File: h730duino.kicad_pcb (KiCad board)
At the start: 4 copper layers, 101.6 x 53.3 mm, 114 parts, among them J1 USB_C_Receptacle_USB2.0, J2 USB_B_Micro, J3 L834-1G1T-91, J4 105162-0001, P1 Digital, P10 CONN_01X01, P11 CONN_01X01, P13 CONN_01X01, P2 Power, P3 Analog, P4 Analog, P5 PWM, P6 PWM, P7 Communication, P8 CONN_01X01, P9 EXT, SW1 RESET, U1 STM32H730ZBT6, U10 APS6404L-3SQN, U12 AP22814BW5, U2 W25Q32JVSS, U3 AP63203WU, U4 AP63205WU, U5 MAX40200AUK, U6 MAX40200AUK, U7 STM32F042F6Px, U8 MAX40200AUK, U9 LAN8742A, Y1 32.768K, Y2 8M, Y3 25M

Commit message: Add SWD connector for cortex-m7, SWD poggo pins and boot jumper for cmsis-dap mcu.
Signed-off-by: Martin Ribelotta <martinribelotta@gmail.com>
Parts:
- added J5: Conn_ARM_JTAG_SWD_10, Connector_PinHeader_1.27mm:PinHeader_2x05_P1.27mm_Vertical_SMD, F.Cu at (153.5, 98.4)
- added J6: Conn_ARM_JTAG_SWD_10, Connector:Tag-Connect_TC2050-IDC-NL_2x05_P1.27mm_Vertical, F.Cu at (142.3, 101.0)
- added JP2: Jumper_NO_Small, Connector_PinHeader_2.54mm:PinHeader_1x02_P2.54mm_Vertical, F.Cu at (131.6, 102.0)
- moved LOGO1 43.6 mm to (192.9, 106.6)
- moved G1 38.6 mm to (194.0, 89.3)
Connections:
- U7 pad 19: (no net) -> /Debug/DBG_SWDIO
- U7 pad 20: (no net) -> /Debug/DBG_SWCK
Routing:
- net /Debug/DBG_SWCK: track 0.00 -> 34.9 mm
- net /Debug/DBG_SWDIO: track 0.00 -> 32.2 mm
- net /Debug/~DBGR: track 4.21 -> 34.7 mm, vias 0 -> 2
- net GND: track 141.4 -> 152.2 mm, vias 74 -> 77
- net /Debug/DBGB: track 5.46 -> 15.7 mm
- net /~RST: track 105.1 -> 114.8 mm, vias 3 -> 4
- net /SWCLK: track 71.9 -> 77.4 mm, vias 2 -> 3
- net +3V3: track 68.4 -> 72.4 mm, vias 28 -> 30
- net /EXT1: track 68.8 -> 64.9 mm
- net /EXT8: track 32.4 -> 28.9 mm
- net /EXT7: track 35.2 -> 31.6 mm
- net /EXT6: track 37.9 -> 34.4 mm
- net /EXT5: track 44.3 -> 40.7 mm
- net /EXT4: track 47.0 -> 43.5 mm
- net /EXT3: track 49.8 -> 46.2 mm
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
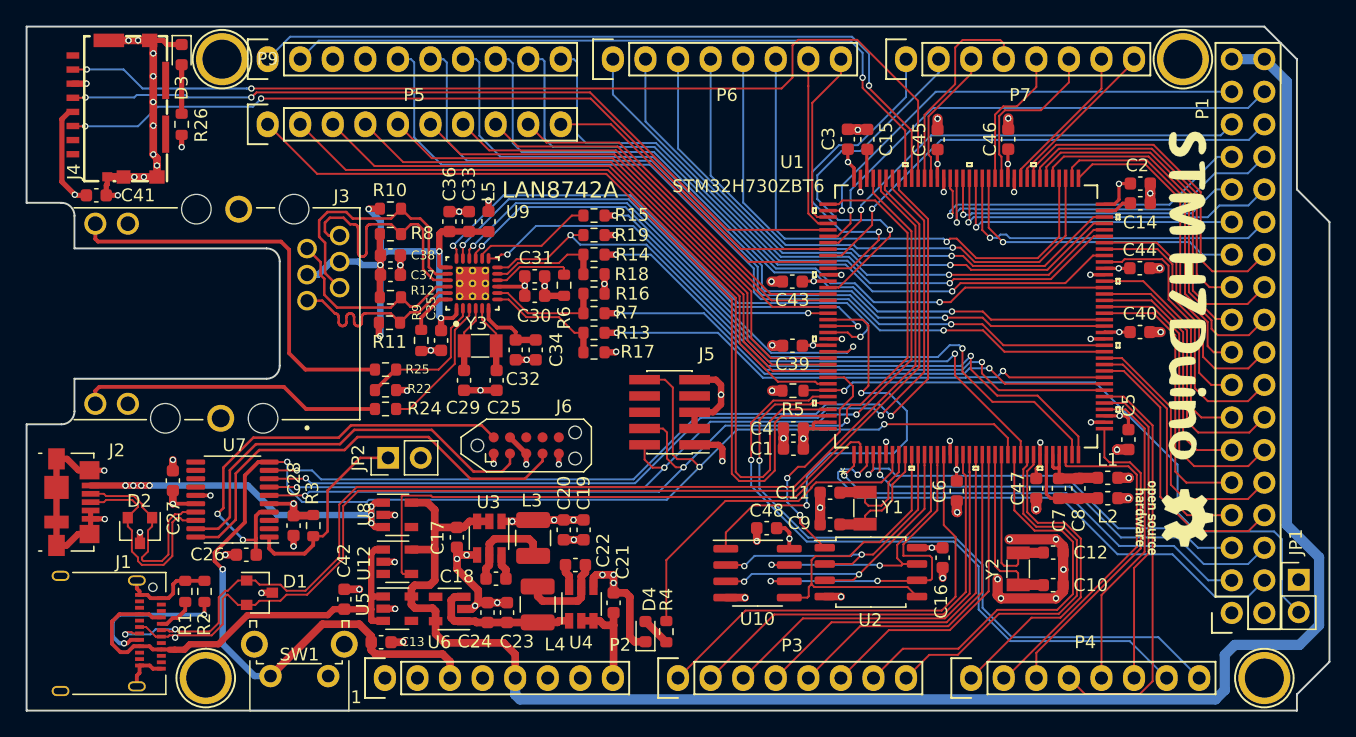
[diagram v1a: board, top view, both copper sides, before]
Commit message: Replace non stocked components.
 - Redesign 5V/3.3V using TPS6216xDSGT
 - Use bigger crystal (move to 5031 case)
 - Change some components parts

Signed-off-by: Martin Ribelotta <martinribelotta@gmail.com>
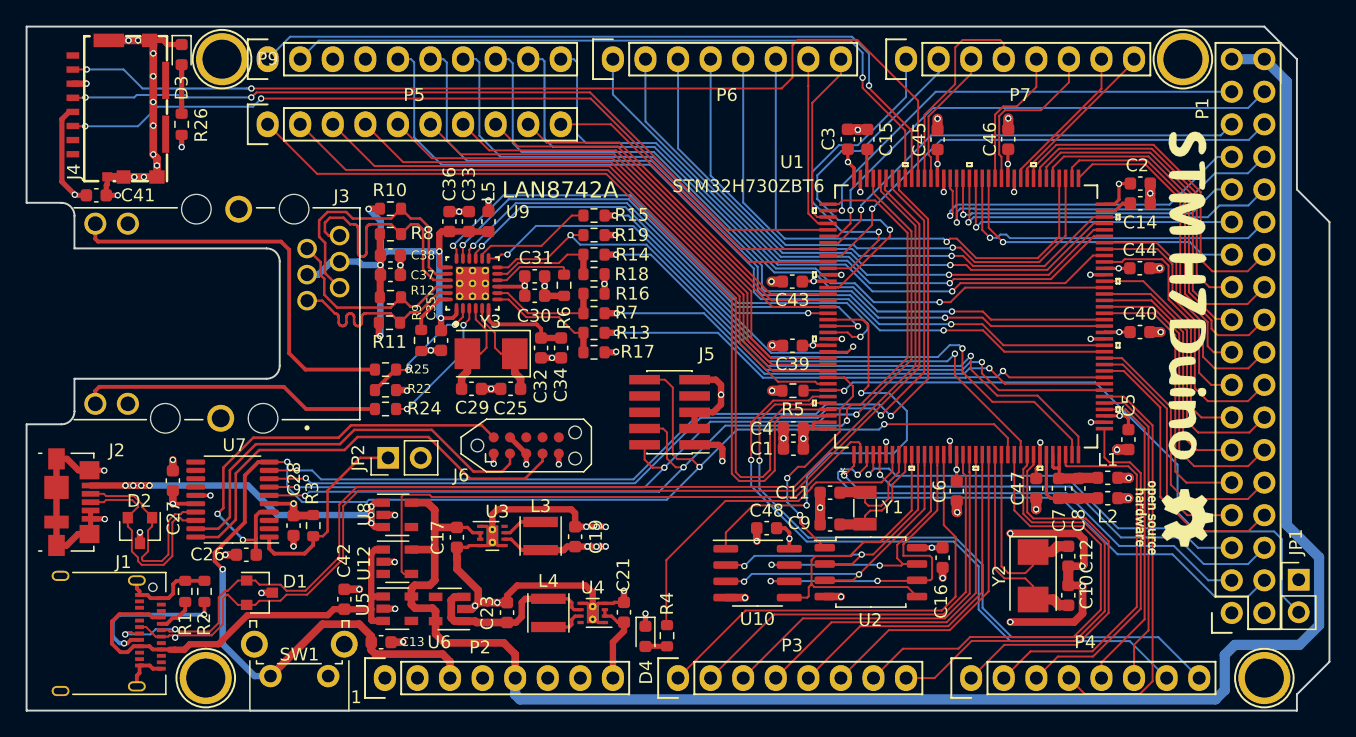
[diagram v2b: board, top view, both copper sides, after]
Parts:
- removed C18, C22: 100n, Capacitor_SMD:C_0603_1608Metric
- removed C20, C24: 2.2u, Capacitor_SMD:C_0603_1608Metric
- C19, C23: value 2.2u -> 22u
- C32: value 420p -> 470p
- L3, L4: value 4.7u -> NR3015T2R2M; footprint Inductor_SMD:L_1210_3225Metric -> Inductor_SMD:L_Taiyo-Yuden_MD-3030
- U3: value AP63203WU -> TPS62162DSG; footprint Package_TO_SOT_SMD:TSOT-23-6 -> Package_SON:WSON-8-1EP_2x2mm_P0.5mm_EP0.9x1.6mm_ThermalVias
- U4: value AP63205WU -> TPS62163DSG; footprint Package_TO_SOT_SMD:TSOT-23-6 -> Package_SON:WSON-8-1EP_2x2mm_P0.5mm_EP0.9x1.6mm_ThermalVias
- Y2, Y3: footprint footprints:Crystal_SMD_3215-2Pin_3.2x1.5mm -> Crystal:Crystal_SMD_5032-2Pin_5.0x3.2mm
- moved C32 1.99 mm to (143.5, 93.4)
- moved C34 1.99 mm to (145.1, 93.4)
- moved C10 1.42 mm to (184.6, 112.7), turned to 90 degrees
- moved Y2 1.28 mm to (181.9, 111.2), turned to 270 degrees
- moved C25 1.28 mm to (141.1, 96.6), turned to 0 degrees
- moved C12 1.21 mm to (184.6, 109.6), turned to 270 degrees
- moved U4 1.13 mm to (147.5, 114.0), turned to 180 degrees
- moved C21 1.10 mm to (150.0, 114.0)
- moved L4 1.07 mm to (144.1, 114.0), turned to 90 degrees
- moved Y3 1.05 mm to (139.6, 93.8), turned to 180 degrees
- moved C29 0.88 mm to (138.1, 96.6), turned to 180 degrees
- moved C19 0.85 mm to (146.2, 108.1), turned to 90 degrees
- moved L3 0.60 mm to (143.5, 108.1), turned to 270 degrees
- moved D4 0.37 mm to (151.6, 115.9), turned to 270 degrees
- moved R4 0.32 mm to (153.3, 115.8)
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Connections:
- L3 pad 1: Net-(C18-Pad1) -> Net-(L3-Pad1)
- L4 pad 1: Net-(C22-Pad1) -> Net-(L4-Pad1)
- U3 pad 1: +3V3 -> GND
- U3 pad 5: Net-(C18-Pad1) -> GND
- U3 pad 6: Net-(C18-Pad2) -> +3V3
- U4 pad 1: /5Vreg -> GND
- U4 pad 5: Net-(C22-Pad1) -> GND
- U4 pad 6: Net-(C22-Pad2) -> /5Vreg
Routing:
- net GND: track 152.2 -> 177.5 mm, vias 77 -> 74
- net Net-(C18-Pad1): track 7.54 -> 0.00 mm
- net Net-(C22-Pad1): track 7.09 -> 0.00 mm
- net /A8: track 25.5 -> 30.4 mm
- net /A7: track 30.1 -> 35.0 mm
- net /A6: track 32.3 -> 37.2 mm
- net Net-(L3-Pad1): track 0.00 -> 3.16 mm
- net Net-(L4-Pad1): track 0.00 -> 3.09 mm
- net Net-(C12-Pad1): track 12.7 -> 15.6 mm
- net Net-(C25-Pad2): track 5.30 -> 8.15 mm
- net /5Vreg: track 11.9 -> 14.7 mm
- net Net-(C29-Pad2): track 5.21 -> 8.03 mm
- net Net-(C10-Pad1): track 13.6 -> 16.4 mm
- net /A9: track 26.9 -> 29.7 mm
- net Net-(C32-Pad1): track 5.55 -> 7.56 mm
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
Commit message: Reorder power supply
Signed-off-by: Martin Ribelotta <martinribelotta@gmail.com>
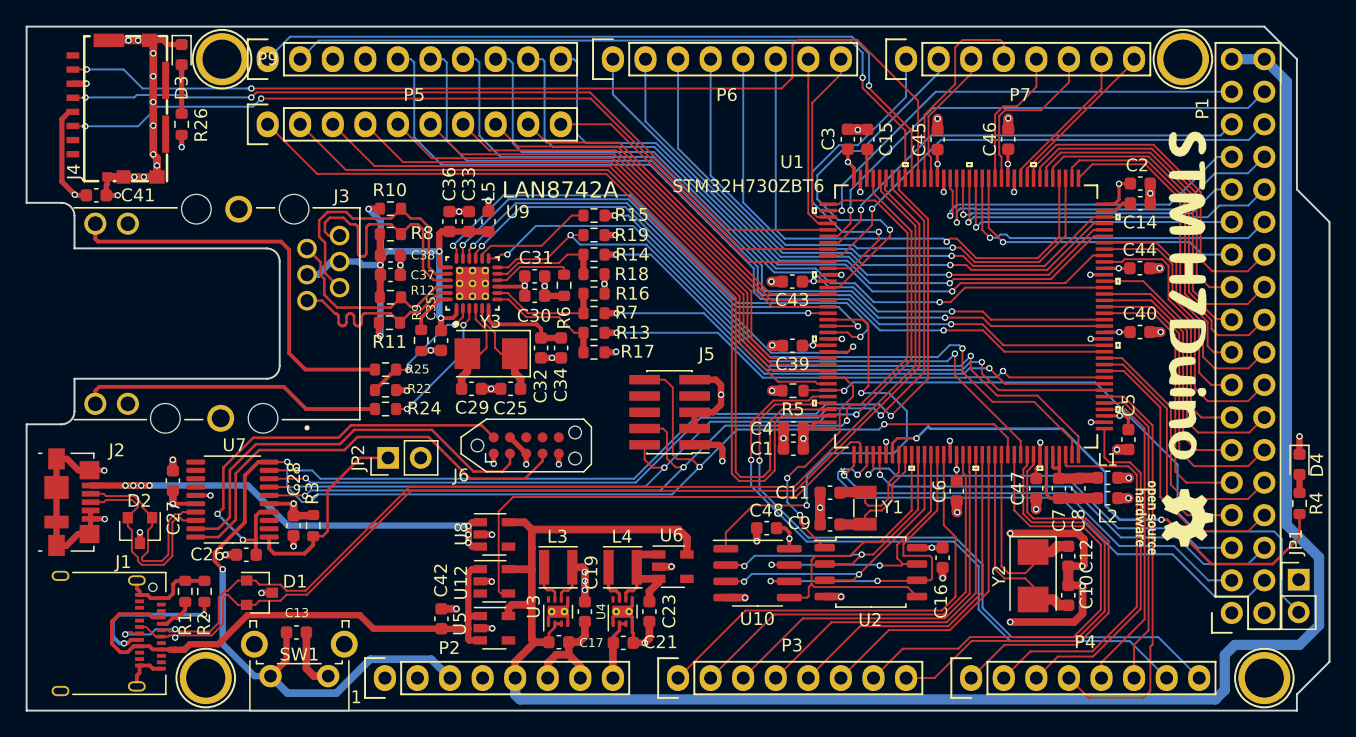
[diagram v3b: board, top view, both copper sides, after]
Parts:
- moved D4 52.7 mm to (202.6, 102.5)
- moved R4 50.4 mm to (202.6, 105.5), turned to 270 degrees
- moved U6 17.7 mm to (153.8, 110.4), turned to 0 degrees
- moved C17 11.4 mm to (144.9, 116.3), turned to 0 degrees
- moved C23 11.1 mm to (151.9, 113.9), turned to 270 degrees
- moved U3 7.81 mm to (144.8, 113.9), turned to 90 degrees
- moved C42 7.72 mm to (135.7, 114.5)
- moved U12 7.72 mm to (139.9, 111.6)
- moved U5 7.72 mm to (139.9, 115.2)
- moved U8 7.72 mm to (139.9, 107.9)
- moved L4 6.80 mm to (149.9, 110.5), turned to 0 degrees
- moved C13 6.65 mm to (124.4, 115.6)
- moved C19 5.89 mm to (146.9, 113.9), turned to 270 degrees
- moved L3 2.80 mm to (144.8, 110.5), turned to 0 degrees
- moved C21 2.39 mm to (149.9, 116.4), turned to 0 degrees
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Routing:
- net GND: track 177.5 -> 162.2 mm, vias 74 -> 69
- net /USR_LED: track 26.9 -> 41.8 mm, vias 0 -> 2
- net /DBG_VBUS: track 29.4 -> 37.3 mm
- net VBUS: track 36.6 -> 44.4 mm
- net /~USB_ON: track 45.3 -> 38.4 mm
- net +5V: track 146.1 -> 152.4 mm
- net /5Vreg: track 14.7 -> 9.52 mm
- net /USB_OTG_HS_P: track 92.9 -> 90.5 mm
- net /USB_OTG_HS_N: track 90.1 -> 87.7 mm
- net /Vin: track 6.90 -> 4.94 mm
- net +3V3: track 74.4 -> 72.6 mm
- net /~RST: track 114.8 -> 116.1 mm
- net /A11: track 32.1 -> 32.7 mm

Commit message: Fix in design:
 - Add r-series to QSPI interfaces
 - Change vCAP from 100n to 2.2u
 - Add pullup to SWCK/DIO and nRST
 - Remove AGND/DGND separation

Signed-off-by: Martin Ribelotta <martinribelotta@gmail.com>
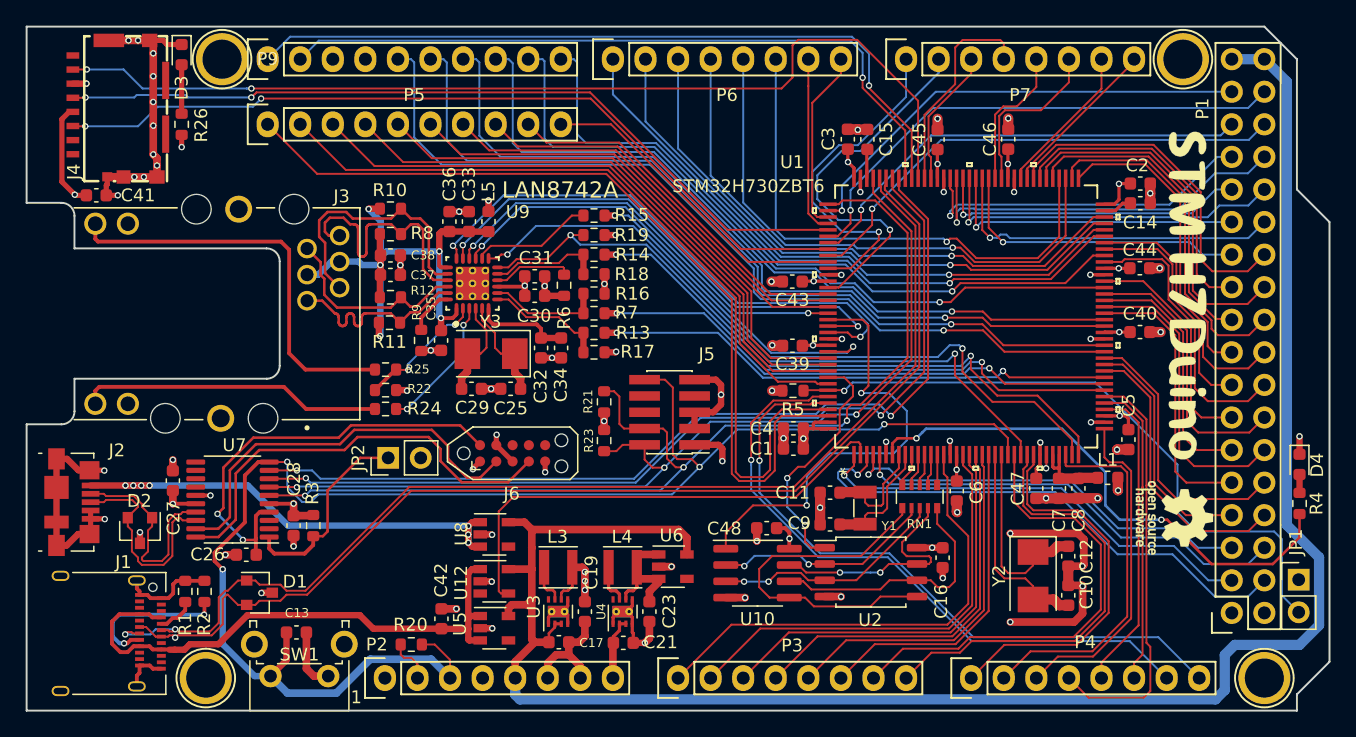
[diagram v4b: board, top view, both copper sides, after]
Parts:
- removed L2: ferrite, Inductor_SMD:L_0603_1608Metric
- added R20: 10K, Resistor_SMD:R_0603_1608Metric, F.Cu at (133.4, 116.5)
- added R21: 10K, Resistor_SMD:R_0603_1608Metric, F.Cu at (148.4, 97.6)
- added R23: 10K, Resistor_SMD:R_0603_1608Metric, F.Cu at (148.4, 100.6)
- added RN1: R_Pack05, Resistor_SMD:R_Array_Convex_5x0603, F.Cu at (173.0, 105.0)
- C14, C15: value 100n -> 2.2u
- R3, R5: value 1K5 -> 10K
- moved J6 1.23 mm to (141.3, 101.6)
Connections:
- C7 pad 2: GNDA -> GND
- C8 pad 2: GNDA -> GND
- U1 pad 10: /OCTOSPIM_P2_IO0 -> Net-(RN1-Pad10)
- U1 pad 11: /OCTOSPIM_P2_IO1 -> Net-(RN1-Pad9)
- U1 pad 12: /OCTOSPIM_P2_IO2 -> Net-(RN1-Pad8)
- U1 pad 13: /OCTOSPIM_P2_IO3 -> Net-(RN1-Pad7)
- U1 pad 14: /OCTOSPIM_P2_CLK -> Net-(RN1-Pad6)
- U1 pad 31: GNDA -> GND
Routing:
- net GNDA: track 7.21 -> 0.00 mm
- net /OCTOSPIM_P2_IO1: track 24.3 -> 17.2 mm
- net /OCTOSPIM_P2_CLK: track 27.0 -> 20.2 mm, vias 2 -> 0
- net /OCTOSPIM_P2_IO2: track 25.0 -> 18.4 mm
- net /SWCLK: track 77.4 -> 83.0 mm
- net +3V3: track 72.6 -> 77.7 mm, vias 30 -> 31
- net GND: track 162.2 -> 166.3 mm, vias 69 -> 70
- net /~RST: track 116.1 -> 120.3 mm
- net /OCTOSPIM_P2_IO3: track 22.6 -> 18.6 mm
- net /SWDIO: track 72.5 -> 75.9 mm
- net Net-(RN1-Pad10): track 0.00 -> 2.68 mm
- net Net-(RN1-Pad9): track 0.00 -> 2.59 mm
- net Net-(RN1-Pad8): track 0.00 -> 2.53 mm
- net Net-(RN1-Pad7): track 0.00 -> 2.47 mm
- net Net-(RN1-Pad6): track 0.00 -> 2.38 mm
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
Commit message: Major rework:
 - Split flash/ram in two QSPI iface
   - Flash is connected to QSPI2
   - PSRAM is connected to QSPI1
 - Move QSPI PSRAM near to P1
 - Reorder pins to P1 and P5
 - Reasign I2C5, UART4 to more convenient place
 - Reasign PWM pins to more convenient place
 - Rerarrange 25MHz ETHPHY crystal

Signed-off-by: Martin Ribelotta <martinribelotta@gmail.com>
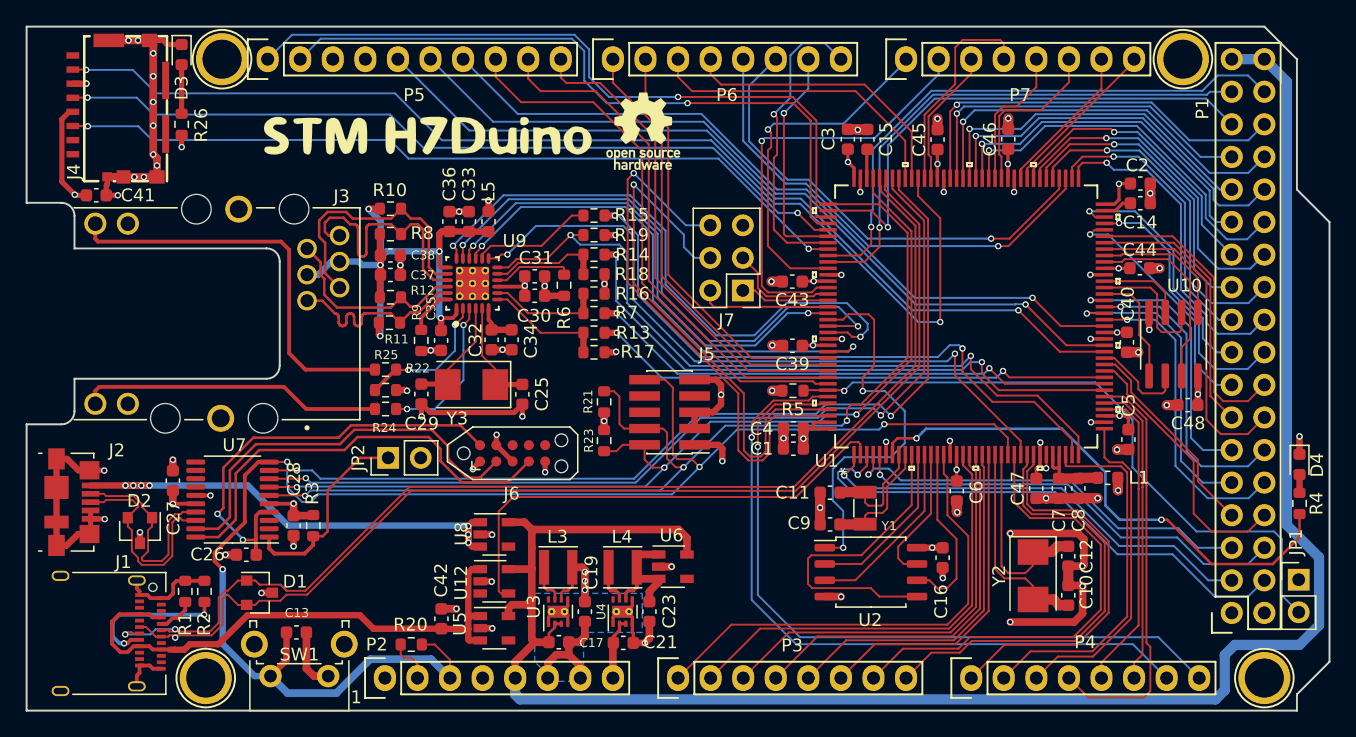
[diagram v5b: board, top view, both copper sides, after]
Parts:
- removed P9: EXT, Socket_Arduino_Mega:Socket_Strip_Arduino_1x10
- removed RN1: R_Pack05, Resistor_SMD:R_Array_Convex_5x0603
- added J7: Conn_02x03_Odd_Even, Connector_PinHeader_2.54mm:PinHeader_2x03_P2.54mm_Vertical, F.Cu at (159.2, 88.9)
- moved G1 60.6 mm to (134.7, 76.8), turned to 0 degrees
- moved LOGO1 51.2 mm to (151.5, 76.5), turned to 0 degrees
- moved U10 37.0 mm to (192.8, 93.1), turned to 270 degrees
- moved C48 34.2 mm to (193.9, 97.8)
- moved C29 3.93 mm to (134.2, 97.0), turned to 90 degrees
- moved C34 3.91 mm to (141.2, 92.7)
- moved C32 3.91 mm to (139.6, 92.7)
- moved Y3 2.85 mm to (138.1, 96.2)
- moved C40 1.29 mm to (189.2, 92.9), turned to 270 degrees
- moved C25 1.01 mm to (142.0, 97.0), turned to 90 degrees
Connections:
- U1 pad 10: Net-(RN1-Pad10) -> /OCTOSPIM_P2_IO0
- U1 pad 100: /I2C5_SCL -> /5(**)
- U1 pad 11: Net-(RN1-Pad9) -> /OCTOSPIM_P2_IO1
- U1 pad 110: /22 -> /24
- U1 pad 111: /0(Rx0) -> /I2C5_SDA
- U1 pad 112: /1(Tx0) -> /I2C5_SCL
- U1 pad 114: /23 -> /1(Tx0)
- U1 pad 115: /24 -> /0(Rx0)
- U1 pad 117: /25 -> /23
- U1 pad 118: /EXT9 -> /22
- U1 pad 12: Net-(RN1-Pad8) -> /OCTOSPIM_P2_IO2
- U1 pad 123: /EXT8 -> /EXT4
- U1 pad 124: /EXT7 -> /EXT3
- U1 pad 125: /EXT6 -> /EXT2
- U1 pad 13: Net-(RN1-Pad7) -> /OCTOSPIM_P2_IO3
- U1 pad 133: /EXT5 -> /6(**)
- U1 pad 134: /EXT4 -> /7(**)
- U1 pad 135: /EXT3 -> /8(**)
- U1 pad 136: /OCTOSPIM_P1_NCS -> /9(**)
- U1 pad 137: /EXT2 -> /10(**)
- U1 pad 14: Net-(RN1-Pad6) -> /OCTOSPIM_P2_CLK
- U1 pad 48: /47 -> /OCTOSPIM_P1_CLK
- U1 pad 54: /10(**) -> /47
- U1 pad 58: /43 -> /OCTOSPIM_P1_IO4
- U1 pad 59: /9(**) -> /OCTOSPIM_P1_IO5
- U1 pad 60: /42 -> /OCTOSPIM_P1_IO6
- U1 pad 63: /41 -> /OCTOSPIM_P1_IO7
- U1 pad 64: /8(**) -> /OCTOSPIM_P1_NCS
- U1 pad 65: /40 -> /43
- U1 pad 66: /39 -> /42
- U1 pad 67: /7(**) -> /41
- U1 pad 68: /6(**) -> /40
- U1 pad 69: /5(**) -> /39
- U1 pad 70: /4(**) -> /38
- U1 pad 73: /38 -> /37
- U1 pad 74: /37 -> /36
- U1 pad 77: /36 -> /35
- U1 pad 78: /35 -> /34
- U1 pad 79: /34 -> /33
- U1 pad 80: /33 -> /32
- U1 pad 87: /32 -> /31
- U1 pad 88: /31 -> /30
- U1 pad 89: /30 -> /29
- U1 pad 90: /29 -> /28
- U1 pad 91: /28 -> /27
- U1 pad 92: /27 -> /26
- U1 pad 93: /26 -> /25
- U1 pad 99: /I2C5_SDA -> /4(**)
- U10 pad 1: /OCTOSPIM_P2_NCS -> /OCTOSPIM_P1_NCS
- U10 pad 2: /OCTOSPIM_P2_IO1 -> /OCTOSPIM_P1_IO5
- U10 pad 3: /OCTOSPIM_P2_IO2 -> /OCTOSPIM_P1_IO6
- U10 pad 5: /OCTOSPIM_P2_IO0 -> /OCTOSPIM_P1_IO4
- U10 pad 6: /OCTOSPIM_P2_CLK -> /OCTOSPIM_P1_CLK
- U10 pad 7: /OCTOSPIM_P2_IO3 -> /OCTOSPIM_P1_IO7
- U2 pad 1: /OCTOSPIM_P1_NCS -> /OCTOSPIM_P2_NCS
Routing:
- net /EXT5: track 40.7 -> 0.00 mm
- net /EXT3: track 46.2 -> 6.97 mm
- net /EXT2: track 49.2 -> 10.3 mm
- net /EXT4: track 43.5 -> 8.64 mm
- net /EXT6: track 34.4 -> 0.00 mm
- net /EXT7: track 31.6 -> 0.00 mm
- net /EXT8: track 28.9 -> 0.00 mm
- net /EXT9: track 25.3 -> 0.00 mm
- net /EXT0: track 67.5 -> 43.3 mm, vias 0 -> 1
- net /EXT1: track 64.9 -> 42.9 mm, vias 0 -> 1
- net /4(**): track 44.3 -> 22.3 mm, vias 1 -> 0
- net /5(**): track 45.6 -> 24.1 mm, vias 1 -> 0
- net /10(**): track 59.5 -> 43.2 mm, vias 1 -> 0
- net /8(**): track 54.3 -> 38.1 mm, vias 1 -> 0
- net /9(**): track 56.8 -> 40.8 mm, vias 1 -> 0
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- added copper zone on B.Cu, net GND
